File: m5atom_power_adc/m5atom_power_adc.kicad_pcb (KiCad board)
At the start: 2 copper layers, 80 x 78 mm, 151 parts, among them J101 USB_C_Receptacle_USB2.0_16P, J102 Conn_01x04_Pin, J103 SubBatt, J104 MainBatt, J105 I2C, J106 Shunt, J107 I2C, J108 I2C, J201 Relay0, J202 R0SW, J301 Relay1, J302 R1SW, J401 Relay2, J402 R2SW, J501 GROVE-CONNECTOR, J601 GROVE-CONNECTOR, Q101 Q_PNP_BEC, Q102 MMBT2222A, Q103 AO3401A, Q201 MMBT2222A, Q301 MMBT2222A, Q401 MMBT2222A, Q501 AO3401A, Q502 MMBT2222A, Q601 AO3401A, Q602 MMBT2222A, Q901 Q_PMOS_GSD, Q902 MMBT2222A, SW101 Boot, SW102 Reset, SW103 Btn0, SW104 Btn1, SW901 Boot, U101 LM2596S-5, U102 AMS1117-3.3, U103 ESP32-S3-MINI-1, U104 AMS1117-3.3, U106 ADS1115IDGS, U107 INA228

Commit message: refactor(m5atom_power_adc): Grove Unitのネットラベルをシルク表記に統一
- LTE_RX/TX/EN・GU_0/1/ENをGU1_0/1/EN・GU0_0/1/ENにリネーム
- 基板シルクの「GU0」「GU1」表記に合わせ、CIRCUIT.mdの記載と整合させる

Co-Authored-By: Claude Sonnet 5 <noreply@anthropic.com>
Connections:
- net /GU_0 renamed /GU1_0
- net /GU_1 renamed /GU1_1
- net /GU_EN renamed /GU1_EN
- net /LTE_EN renamed /GU0_EN
- net /LTE_RX renamed /GU0_0
- net /LTE_TX renamed /GU0_1
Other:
- board text added: "GU0"
- board text added: "GU1"
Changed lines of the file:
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@@
 	(net 22 "Net-(D401-A)")
 	(net 23 "Net-(D402-A)")
-	(net 24 "/GU_0")
-	(net 25 "/GU_1")
-	(net 26 "/LTE_RX")
-	(net 27 "/LTE_TX")
+	(net 24 "/GU1_0")
+	(net 25 "/GU1_1")
+	(net 26 "/GU0_0")
+	(net 27 "/GU0_1")
 	(net 28 "Net-(J101-CC1)")
 	(net 29 "unconnected-(J101-SBU1-PadA8)")
@@
 	(net 43 "/Relay1")
 	(net 44 "/Relay2")
-	(net 45 "/GU_EN")
-	(net 46 "/LTE_EN")
+	(net 45 "/GU1_EN")
+	(net 46 "/GU0_EN")
 	(net 47 "unconnected-(U103-IO41-Pad37)")
 	(net 48 "unconnected-(U103-IO39-Pad35)")
@@
 			(layers "F.Cu" "F.Mask" "F.Paste")
 			(roundrect_rratio 0.25)
-			(net 45 "/GU_EN")
+			(net 45 "/GU1_EN")
 			(pintype "passive")
 		)
@@
 			(layers "F.Cu" "F.Mask" "F.Paste")
 			(roundrect_rratio 0.25)
-			(net 24 "/GU_0")
+			(net 24 "/GU1_0")
 			(pinfunction "A1")
 			(pintype "passive")
@@
 			(layers "F.Cu" "F.Mask" "F.Paste")
 			(roundrect_rratio 0.25)
-			(net 25 "/GU_1")
+			(net 25 "/GU1_1")
 			(pinfunction "A1")
 			(pintype "passive")
@@
 			(layers "F.Cu" "F.Mask" "F.Paste")
 			(roundrect_rratio 0.25)
-			(net 26 "/LTE_RX")
+			(net 26 "/GU0_0")
 			(pinfunction "A1")
 			(pintype "passive")
@@
 			(layers "F.Cu" "F.Mask" "F.Paste")
 			(roundrect_rratio 0.25)
-			(net 27 "/LTE_TX")
+			(net 27 "/GU0_1")
 			(pinfunction "A1")
 			(pintype "passive")
@@
 			(size 0.8 0.4)
 			(layers "F.Cu" "F.Mask" "F.Paste")
-			(net 26 "/LTE_RX")
+			(net 26 "/GU0_0")
 			(pinfunction "IO4")
 			(pintype "bidirectional")
@@
 			(size 0.8 0.4)
 			(layers "F.Cu" "F.Mask" "F.Paste")
-			(net 27 "/LTE_TX")
+			(net 27 "/GU0_1")
 			(pinfunction "IO5")
 			(pintype "bidirectional")
@@
 			(size 0.8 0.4)
 			(layers "F.Cu" "F.Mask" "F.Paste")
-			(net 46 "/LTE_EN")
+			(net 46 "/GU0_EN")
 			(pinfunction "IO6")
 			(pintype "bidirectional")
@@
 			(size 0.8 0.4)
 			(layers "F.Cu" "F.Mask" "F.Paste")
-			(net 24 "/GU_0")
+			(net 24 "/GU1_0")
 			(pinfunction "IO7")
 			(pintype "bidirectional")
@@
 			(size 0.8 0.4)
 			(layers "F.Cu" "F.Mask" "F.Paste")
-			(net 25 "/GU_1")
+			(net 25 "/GU1_1")
 			(pinfunction "IO8")
 			(pintype "bidirectional")
@@
 			(size 0.8 0.4)
 			(layers "F.Cu" "F.Mask" "F.Paste")
-			(net 45 "/GU_EN")
+			(net 45 "/GU1_EN")
 			(pinfunction "IO9")
 			(pintype "bidirectional")
@@
 			(layers "F.Cu" "F.Mask" "F.Paste")
 			(roundrect_rratio 0.25)
-			(net 46 "/LTE_EN")
+			(net 46 "/GU0_EN")
 			(pintype "passive")
 		)
@@
 			(layers "*.Cu" "*.Mask")
 			(remove_unused_layers no)
-			(net 27 "/LTE_TX")
+			(net 27 "/GU0_1")
 			(pinfunction "3")
 			(pintype "bidirectional")
@@
 			(layers "*.Cu" "*.Mask")
 			(remove_unused_layers no)
-			(net 26 "/LTE_RX")
+			(net 26 "/GU0_0")
 			(pinfunction "4")
 			(pintype "bidirectional")
@@
 			(layers "*.Cu" "*.Mask")
 			(remove_unused_layers no)
-			(net 25 "/GU_1")
+			(net 25 "/GU1_1")
 			(pinfunction "3")
 			(pintype "bidirectional")
@@
 			(layers "*.Cu" "*.Mask")
 			(remove_unused_layers no)
-			(net 24 "/GU_0")
+			(net 24 "/GU1_0")
 			(pinfunction "4")
 			(pintype "bidirectional")
@@
 		)
 	)
+	(gr_text "GU1"
+		(at 81.305 113.691 0)
+		(layer "F.SilkS")
+		(effects
+			(font
+				(size 1 1)
+				(thickness 0.15)
+			)
+			(justify left bottom)
+		)
+	)
 	(gr_text "TX"
 		(at 130.605 46.963 315)
@@
 		(layer "F.SilkS")
 		(effects
+			(font
+				(size 1 1)
+				(thickness 0.15)
+			)
+			(justify left bottom)
+		)
+	)
+	(gr_text "GU0"
+		(at 66.055 113.691 0)
+		(layer "F.SilkS")
+		(effects

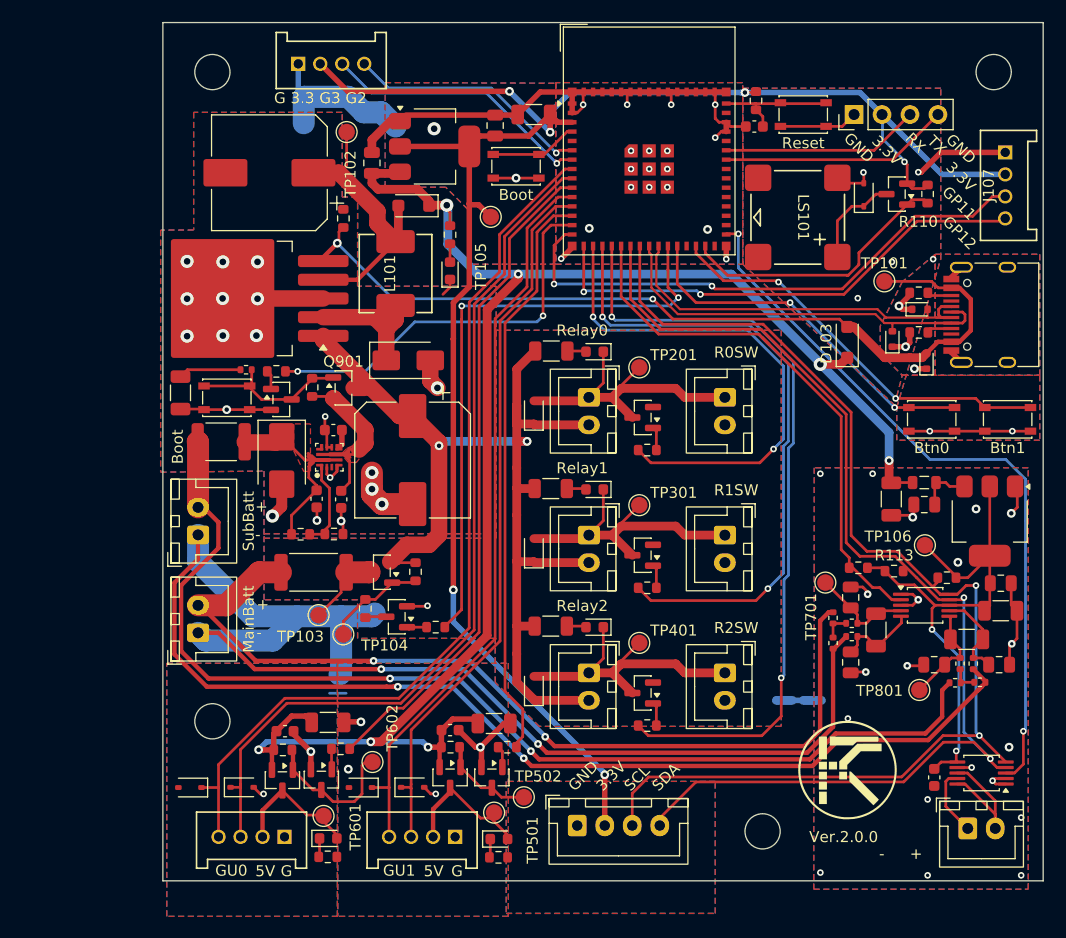
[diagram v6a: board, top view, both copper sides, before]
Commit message: feat: ACC検知回路（IGN連動deep sleep復帰用）を追加
分圧を使わず、車のACC(12V)をD109(BZT52C15ツェナー保護)→Q105(PDTC114YU,115デジタルトランジスタ)→R111(10kΩプルアップ)経由でGPIO1に直接入力する回路を追加。ACC ONでGPIO1がLOWになり、ext1 wakeup(ANY_LOW)でdeep sleepから復帰させる想定。

- GPIO1はstrapping pinに該当せずRTC GPIO対応のため採用
- コネクタ用スペースがなくスルーホールパッド1点で対応、GND側はNetTieで共通化済みのGND1を流用し省略
- Q105のEmitterは配線都合でGND2ではなくGND1に接続
- ファームウェア未実装。電源保持・理想ダイオード回路の検証用テストボード製造・テストを先に行う方針

Co-Authored-By: Claude Sonnet 5 <noreply@anthropic.com>
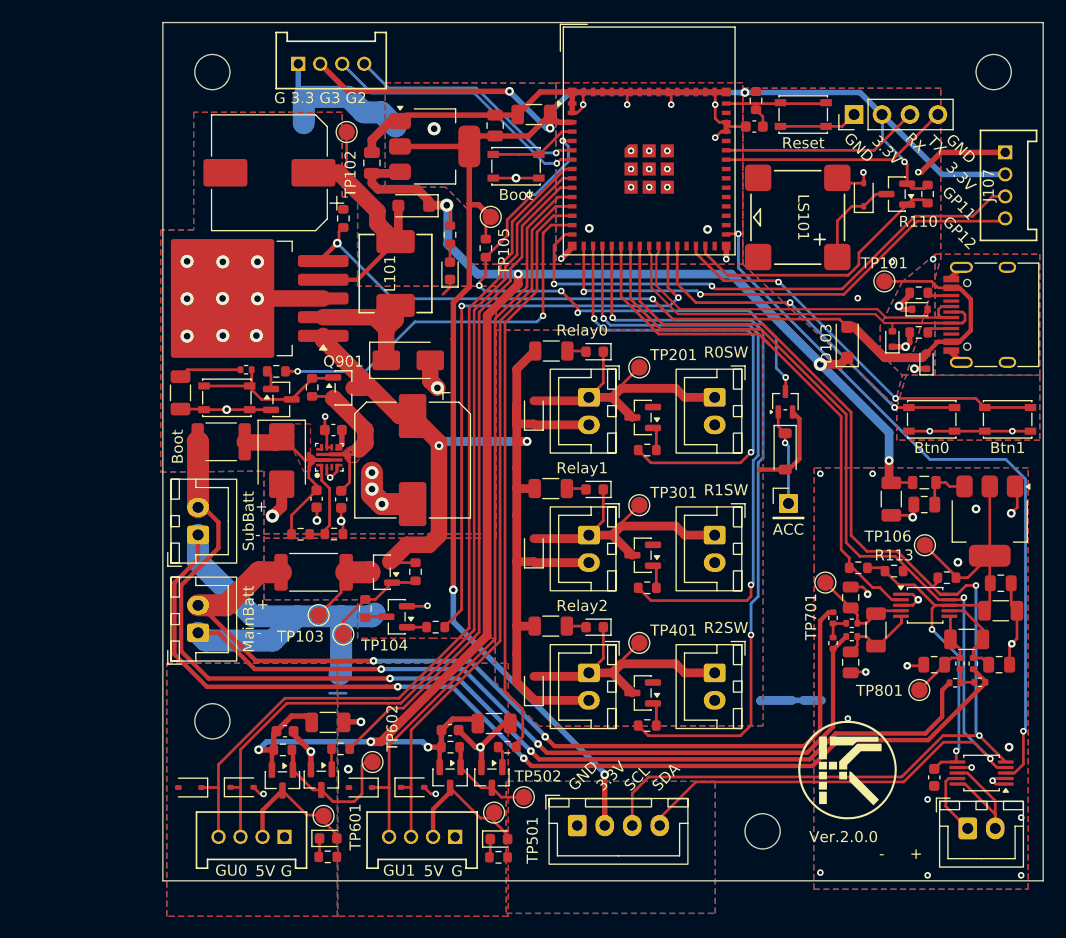
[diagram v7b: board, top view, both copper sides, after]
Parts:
- added D109: BZT52Bxx, Diode_SMD:D_SOD-123, F.Cu at (117.9, 75.0)
- added J109: ACC, Connector_PinHeader_2.54mm:PinHeader_1x01_P2.54mm_Vertical, F.Cu at (118.2, 79.7)
- added Q105: PDTC114YU,115, Package_TO_SOT_SMD:SOT-323_SC-70, F.Cu at (117.9, 70.5)
- added R111: 10k, Resistor_SMD:R_0603_1608Metric, F.Cu at (90.7, 56.5)
- moved J202 0.92 mm to (111.5, 70.1)
- moved J302 0.92 mm to (111.5, 82.6)
- moved J402 0.92 mm to (111.5, 95.1)
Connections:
- U103 pad 5: unconnected-(U103-IO1-Pad5) -> /CAR_ACC
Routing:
- net /CAR_ACC: track 0.00 -> 52.6 mm, vias 0 -> 6
- net GND1: track 75.6 -> 85.6 mm
- net /ACC: track 0.00 -> 8.80 mm, vias 0 -> 1
- net /Relay2: track 71.4 -> 68.0 mm
- net /Relay0: track 46.9 -> 43.6 mm
- net /Relay1: track 59.0 -> 56.3 mm
- net +3.3V: track 170.8 -> 172.1 mm
- net Net-(D401-A): track 28.2 -> 27.3 mm
- net Net-(D301-A): track 28.2 -> 27.3 mm
- net Net-(D201-A): track 28.2 -> 27.3 mm
